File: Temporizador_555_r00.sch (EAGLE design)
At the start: 9 parts, among them IC1 LM555

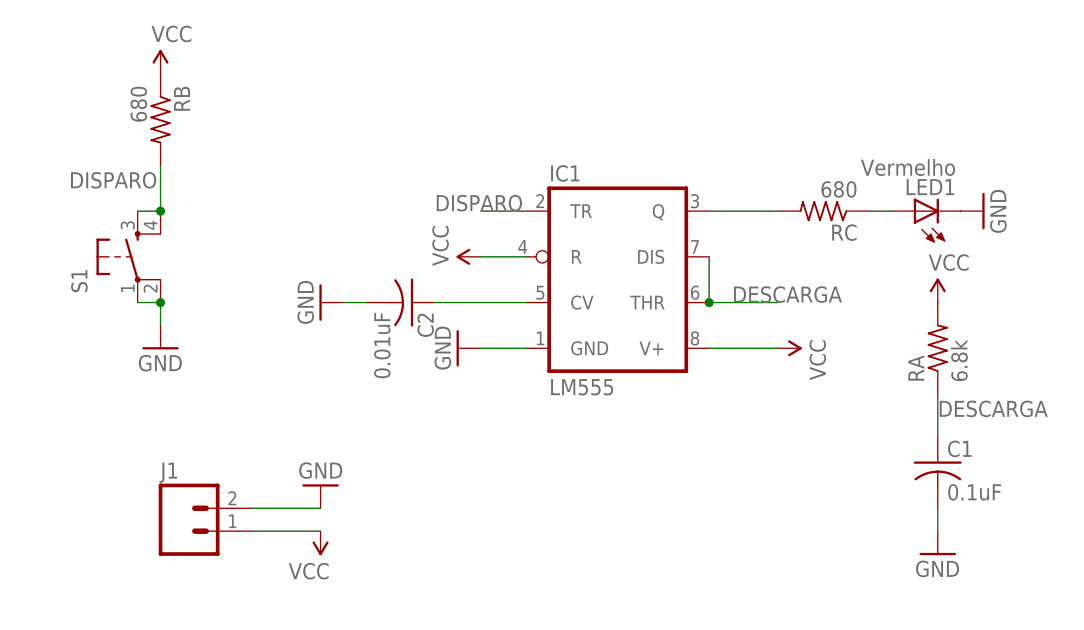
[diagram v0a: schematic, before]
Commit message: Primeira revisao (r00) e arquivos para fabricacao
Primeira revisao (estética e troca do conector da fonte por um KRE 5mm).
Gerados Gerber para fabricaçao da PCI
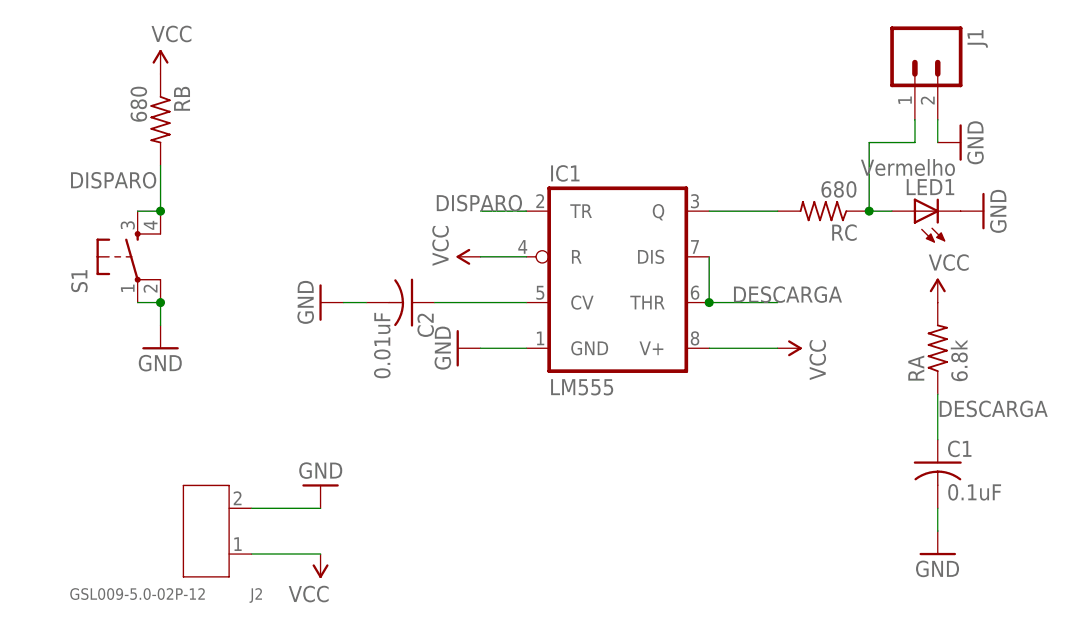
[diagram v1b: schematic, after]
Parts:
- added J2: GSL009-5.0-02P-12, Seeed-OPL-Connector:SCREW-TERMINAL-BLUE(2P-5.0)
- J1: device SparkFun-Connectors:M02POLAR -> SparkFun-Connectors:M02PTH
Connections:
- net GND: now also J2.2
- net N$3: now also J1.1
- net VCC: now also J2.1; no longer J1.1
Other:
- moved on the sheet: J1
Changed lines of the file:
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@@
 <layer number="115" name="ReferenceISLANDS" color="7" fill="1" visible="yes" active="yes"/>
 <layer number="116" name="Patch_BOT" color="9" fill="4" visible="no" active="yes"/>
+<layer number="117" name="BACKMAAT1" color="7" fill="1" visible="no" active="no"/>
 <layer number="118" name="Rect_Pads" color="7" fill="1" visible="no" active="no"/>
+<layer number="119" name="KAP_TEKEN" color="7" fill="1" visible="no" active="no"/>
+<layer number="120" name="KAP_MAAT1" color="7" fill="1" visible="no" active="no"/>
 <layer number="121" name="_tsilk" color="7" fill="1" visible="no" active="yes"/>
 <layer number="122" name="_bsilk" color="7" fill="1" visible="no" active="yes"/>
@@
 <layer number="128" name="_bValues" color="7" fill="1" visible="no" active="yes"/>
 <layer number="129" name="Mask" color="7" fill="1" visible="yes" active="yes"/>
+<layer number="130" name="SMDSTROOK" color="7" fill="1" visible="no" active="no"/>
 <layer number="131" name="tAdjust" color="7" fill="1" visible="no" active="yes"/>
 <layer number="132" name="bAdjust" color="7" fill="1" visible="no" active="yes"/>
+<layer number="133" name="bottom_silk" color="7" fill="1" visible="no" active="no"/>
 <layer number="144" name="Drill_legend" color="7" fill="1" visible="no" active="yes"/>
 <layer number="150" name="Notes" color="7" fill="1" visible="no" active="yes"/>
@@
 <part name="C1" library="adafruit" deviceset="C-US" device="050-024X044" value="0.1uF"/>
 <part name="GND4" library="SparkFun-Aesthetics" deviceset="GND" device=""/>
-<part name="J1" library="SparkFun-Connectors" deviceset="M02" device="POLAR"/>
 <part name="SUPPLY4" library="SparkFun-Aesthetics" deviceset="VCC" device=""/>
 <part name="GND5" library="SparkFun-Aesthetics" deviceset="GND" device=""/>
@@
 <part name="S1" library="GeekAmmo" deviceset="TACTILE-SWITCH" device="-PTH"/>
 <part name="GND6" library="SparkFun-Aesthetics" deviceset="GND" device=""/>
+<part name="J1" library="SparkFun-Connectors" deviceset="M02" device="PTH"/>
+<part name="GND7" library="SparkFun-Aesthetics" deviceset="GND" device=""/>
+<part name="J2" library="Seeed-OPL-Connector" deviceset="SCREW-TERMINAL-BLUE(2P-5.0)" device="" value="GSL009-5.0-02P-12"/>
 </parts>
 <sheets>
@@
 <instance part="C1" gate="G$1" x="93.98" y="17.78"/>
 <instance part="GND4" gate="1" x="93.98" y="7.62"/>
-<instance part="J1" gate="G$1" x="10.16" y="10.16"/>
-<instance part="SUPPLY4" gate="G$1" x="25.4" y="10.16" rot="R180"/>
+<instance part="SUPPLY4" gate="G$1" x="25.4" y="7.62" rot="R180"/>
 <instance part="GND5" gate="1" x="25.4" y="15.24" rot="R180"/>
 <instance part="RB" gate="G$1" x="7.62" y="55.88" rot="R270"/>
@@
 </instance>
 <instance part="GND6" gate="1" x="7.62" y="30.48"/>
+<instance part="J1" gate="G$1" x="91.44" y="63.5" rot="R270"/>
+<instance part="GND7" gate="1" x="96.52" y="53.34" rot="R90"/>
+<instance part="J2" gate="G$1" x="12.7" y="10.16" rot="R180"/>
 </instances>
 <busses>
@@
 </segment>
 <segment>
-<pinref part="J1" gate="G$1" pin="1"/>
 <pinref part="SUPPLY4" gate="G$1" pin="VCC"/>
-<wire x1="25.4" y1="10.16" x2="17.78" y2="10.16" width="0.1524" layer="91"/>
+<wire x1="25.4" y1="7.62" x2="17.78" y2="7.62" width="0.1524" layer="91"/>
+<pinref part="J2" gate="G$1" pin="1"/>
 </segment>
 <segment>
@@
 </segment>
 <segment>
-<pinref part="J1" gate="G$1" pin="2"/>
 <pinref part="GND5" gate="1" pin="GND"/>
 <wire x1="25.4" y1="12.7" x2="17.78" y2="12.7" width="0.1524" layer="91"/>
+<pinref part="J2" gate="G$1" pin="2"/>
 </segment>
 <segment>
@@
 <junction x="7.62" y="35.56"/>
 </segment>
+<segment>
+<pinref part="J1" gate="G$1" pin="2"/>
+<pinref part="GND7" gate="1" pin="GND"/>
+<wire x1="93.98" y1="53.34" x2="93.98" y2="55.88" width="0.1524" layer="91"/>
+</segment>
 </net>
 <net name="N$3" class="0">
@@
 <pinref part="RC" gate="G$1" pin="1"/>
 <wire x1="88.9" y1="45.72" x2="86.36" y2="45.72" width="0.1524" layer="91"/>
-</segment>
-</net>
+<pinref part="J1" gate="G$1" pin="1"/>
+<wire x1="91.44" y1="55.88" x2="91.44" y2="53.34" width="0.1524" layer="91"/>
+<wire x1="91.44" y1="53.34" x2="86.36" y2="53.34" width="0.1524" layer="91"/>
+<wire x1="86.36" y1="53.34" x2="86.36" y2="45.72" width="0.1524" layer="91"/>
+<junction x="86.36" y="45.72"/>
+</segment>
+</net>

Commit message: Upload de arquivos atuais que foram para produção
Upload de arquivos atuais que foram para produção
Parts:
- C1: value 0.1uF -> 10uF
- RA: value 6.8k -> 470k
- RB, RC: value 680 -> 1k
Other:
- moved on the sheet: J2, RB, S1
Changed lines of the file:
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@@
 <part name="GND1" library="SparkFun-Aesthetics" deviceset="GND" device=""/>
 <part name="GND2" library="SparkFun-Aesthetics" deviceset="GND" device=""/>
-<part name="RA" library="adafruit" deviceset="R-US_" device="0207/10" value="6.8k"/>
-<part name="RC" library="adafruit" deviceset="R-US_" device="0207/10" value="680"/>
+<part name="RA" library="adafruit" deviceset="R-US_" device="0207/10" value="470k"/>
+<part name="RC" library="adafruit" deviceset="R-US_" device="0207/10" value="1k"/>
 <part name="LED1" library="adafruit" deviceset="LED" device="5MM" value="Vermelho"/>
 <part name="SUPPLY3" library="SparkFun-Aesthetics" deviceset="VCC" device=""/>
 <part name="GND3" library="SparkFun-Aesthetics" deviceset="GND" device=""/>
-<part name="C1" library="adafruit" deviceset="C-US" device="050-024X044" value="0.1uF"/>
+<part name="C1" library="adafruit" deviceset="C-US" device="050-024X044" value="10uF"/>
 <part name="GND4" library="SparkFun-Aesthetics" deviceset="GND" device=""/>
 <part name="SUPPLY4" library="SparkFun-Aesthetics" deviceset="VCC" device=""/>
 <part name="GND5" library="SparkFun-Aesthetics" deviceset="GND" device=""/>
-<part name="RB" library="adafruit" deviceset="R-US_" device="0207/10" value="680"/>
+<part name="RB" library="adafruit" deviceset="R-US_" device="0207/10" value="1k"/>
 <part name="SUPPLY5" library="SparkFun-Aesthetics" deviceset="VCC" device=""/>
 <part name="S1" library="GeekAmmo" deviceset="TACTILE-SWITCH" device="-PTH"/>
@@
 <instance part="C2" gate="G$1" x="35.56" y="35.56" rot="R270"/>
 <instance part="GND1" gate="1" x="40.64" y="30.48" rot="R270"/>
-<instance part="GND2" gate="1" x="25.4" y="35.56" rot="R270"/>
+<instance part="GND2" gate="1" x="27.94" y="33.02"/>
 <instance part="RA" gate="G$1" x="93.98" y="30.48" rot="R90"/>
 <instance part="RC" gate="G$1" x="81.28" y="45.72" rot="R180"/>
@@
 <instance part="C1" gate="G$1" x="93.98" y="17.78"/>
 <instance part="GND4" gate="1" x="93.98" y="7.62"/>
-<instance part="SUPPLY4" gate="G$1" x="25.4" y="7.62" rot="R180"/>
-<instance part="GND5" gate="1" x="25.4" y="15.24" rot="R180"/>
-<instance part="RB" gate="G$1" x="7.62" y="55.88" rot="R270"/>
-<instance part="SUPPLY5" gate="G$1" x="7.62" y="60.96"/>
-<instance part="S1" gate="G$1" x="5.08" y="40.64" smashed="yes" rot="R90">
-<attribute name="NAME" x="-0.508" y="36.576" size="1.778" layer="95" rot="R90"/>
+<instance part="SUPPLY4" gate="G$1" x="76.2" y="12.7" rot="R180"/>
+<instance part="GND5" gate="1" x="76.2" y="20.32" rot="R180"/>
+<instance part="RB" gate="G$1" x="20.32" y="45.72" rot="R270"/>
+<instance part="SUPPLY5" gate="G$1" x="20.32" y="50.8"/>
+<instance part="S1" gate="G$1" x="17.78" y="30.48" smashed="yes" rot="R90">
+<attribute name="NAME" x="12.192" y="26.416" size="1.778" layer="95" rot="R90"/>
 </instance>
-<instance part="GND6" gate="1" x="7.62" y="30.48"/>
+<instance part="GND6" gate="1" x="20.32" y="20.32"/>
 <instance part="J1" gate="G$1" x="91.44" y="63.5" rot="R270"/>
 <instance part="GND7" gate="1" x="96.52" y="53.34" rot="R90"/>
-<instance part="J2" gate="G$1" x="12.7" y="10.16" rot="R180"/>
+<instance part="J2" gate="G$1" x="63.5" y="15.24" rot="R180"/>
 </instances>
 <busses>
@@
 <segment>
 <pinref part="SUPPLY4" gate="G$1" pin="VCC"/>
-<wire x1="25.4" y1="7.62" x2="17.78" y2="7.62" width="0.1524" layer="91"/>
+<wire x1="76.2" y1="12.7" x2="68.58" y2="12.7" width="0.1524" layer="91"/>
 <pinref part="J2" gate="G$1" pin="1"/>
 </segment>
@@
 <segment>
 <pinref part="GND5" gate="1" pin="GND"/>
-<wire x1="25.4" y1="12.7" x2="17.78" y2="12.7" width="0.1524" layer="91"/>
+<wire x1="76.2" y1="17.78" x2="68.58" y2="17.78" width="0.1524" layer="91"/>
 <pinref part="J2" gate="G$1" pin="2"/>
 </segment>
@@
 <pinref part="S1" gate="G$1" pin="1"/>
 <pinref part="S1" gate="G$1" pin="2"/>
-<wire x1="5.08" y1="35.56" x2="7.62" y2="35.56" width="0.1524" layer="91"/>
+<wire x1="17.78" y1="25.4" x2="20.32" y2="25.4" width="0.1524" layer="91"/>
 <pinref part="GND6" gate="1" pin="GND"/>
-<wire x1="7.62" y1="35.56" x2="7.62" y2="33.02" width="0.1524" layer="91"/>
-<junction x="7.62" y="35.56"/>
+<wire x1="20.32" y1="25.4" x2="20.32" y2="22.86" width="0.1524" layer="91"/>
+<junction x="20.32" y="25.4"/>
 </segment>
 <segment>
@@
 <pinref part="S1" gate="G$1" pin="3"/>
 <pinref part="S1" gate="G$1" pin="4"/>
-<wire x1="5.08" y1="45.72" x2="7.62" y2="45.72" width="0.1524" layer="91"/>
+<wire x1="17.78" y1="35.56" x2="20.32" y2="35.56" width="0.1524" layer="91"/>
 <pinref part="RB" gate="G$1" pin="2"/>
-<wire x1="7.62" y1="45.72" x2="7.62" y2="50.8" width="0.1524" layer="91"/>
-<junction x="7.62" y="45.72"/>
-<label x="-2.54" y="48.26" size="1.778" layer="95"/>
+<wire x1="20.32" y1="35.56" x2="20.32" y2="40.64" width="0.1524" layer="91"/>
+<junction x="20.32" y="35.56"/>
+<label x="10.16" y="38.1" size="1.778" layer="95"/>
 </segment>
 </net>
